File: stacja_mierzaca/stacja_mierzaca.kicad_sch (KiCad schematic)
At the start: 4 parts, among them U1 ESP32-WROOM-32, U2 DS18B20, U3 Ai-Thinker-Ra-02

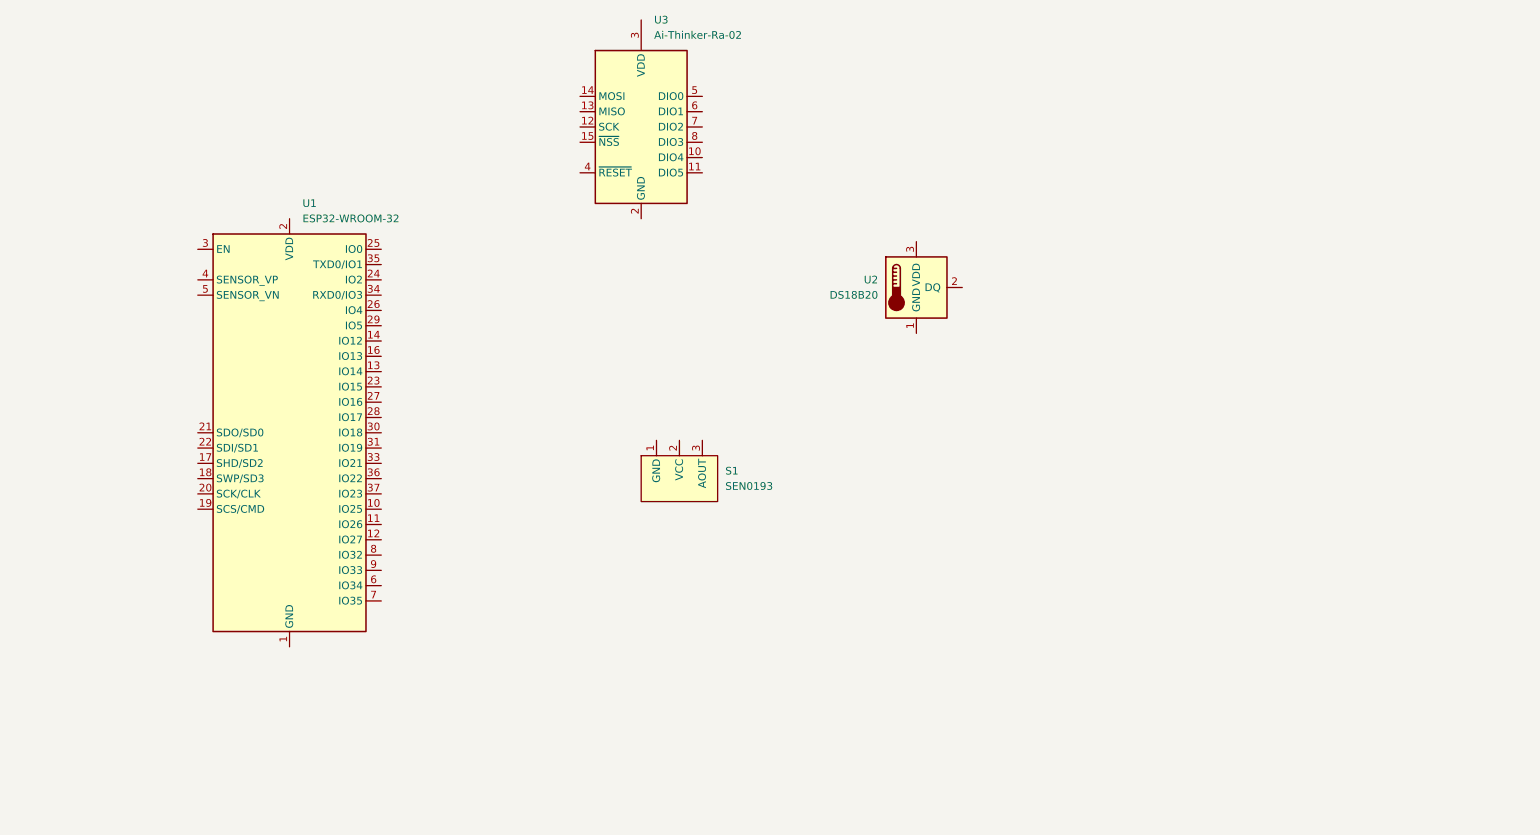
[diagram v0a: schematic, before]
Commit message: feat: add custom esp32 symbol
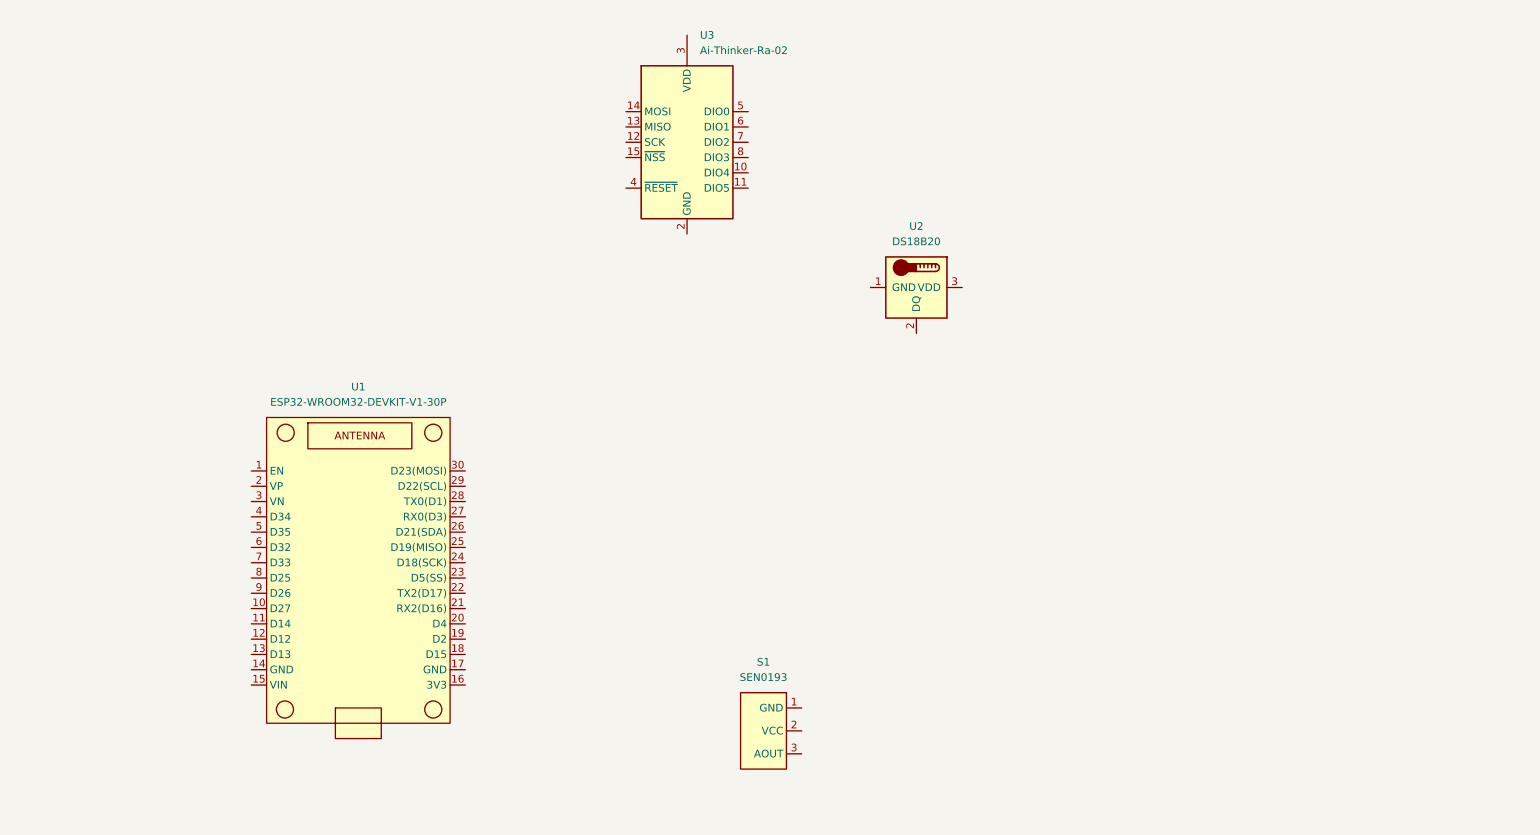
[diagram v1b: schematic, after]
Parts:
- removed U1: ESP32-WROOM-32, RF_Module:ESP32-S2-WROVER, symbol RF_Module:ESP32-WROOM-32
- added U1: ESP32-WROOM32-DEVKIT-V1-30P, symbol custom_sensors:ESP32-WROOM32-DEVKIT-V1-30P
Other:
- moved on the sheet: S1, U2, U3

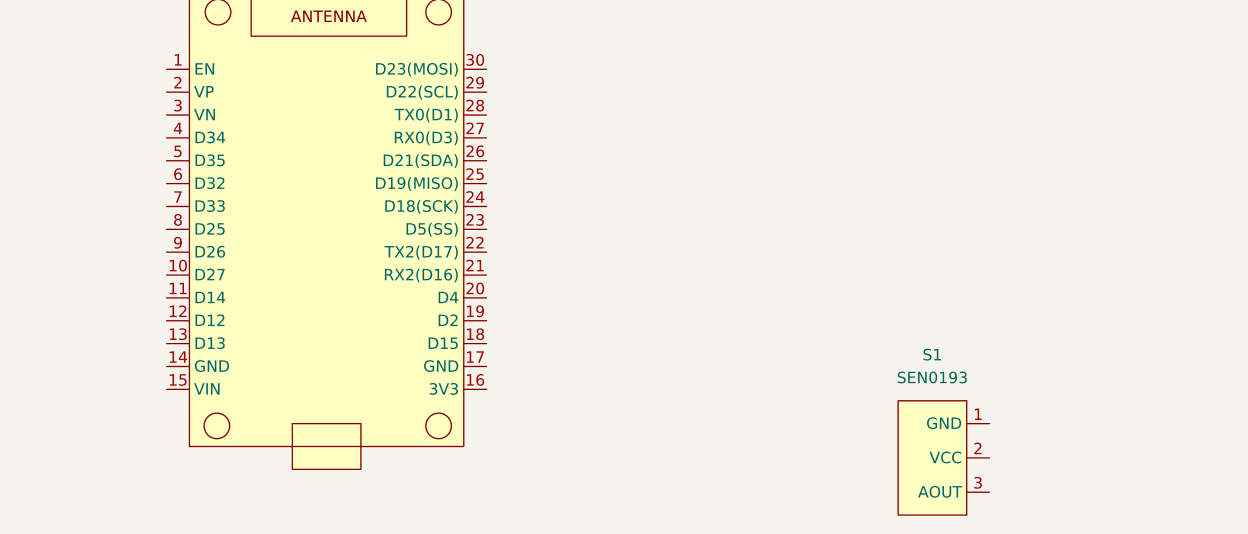
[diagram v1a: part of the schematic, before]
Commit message: feat: connect moisture sensor
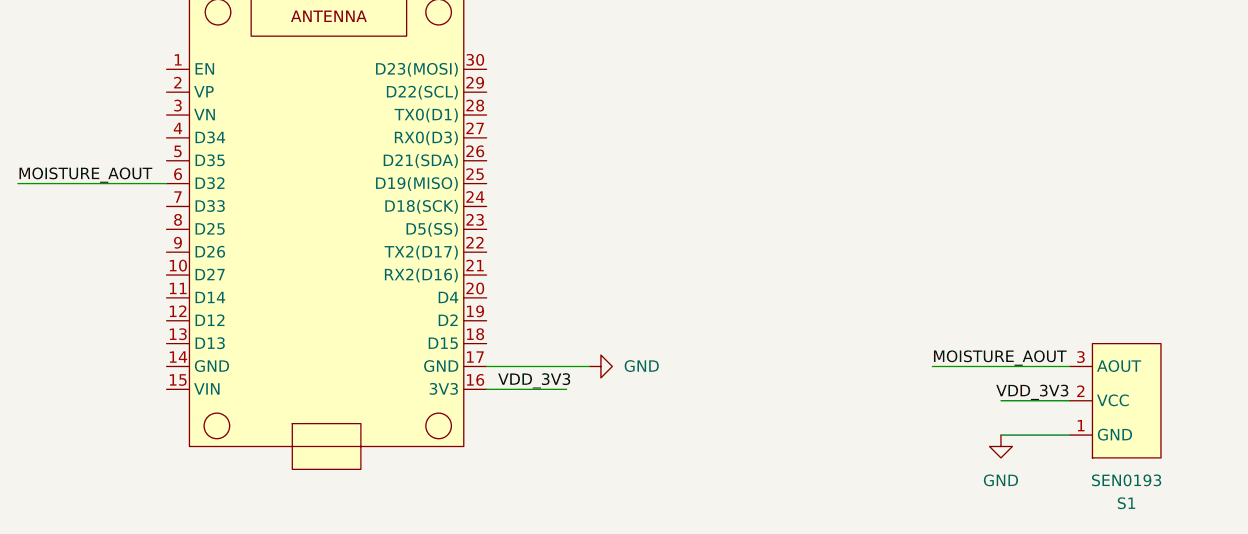
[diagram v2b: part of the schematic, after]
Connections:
- net GND: now reaches S1.1 (GND)
- net GND: now also U1.17 (GND)
- net VDD_3V3: now reaches S1.2 (VCC)
- net VDD_3V3: now also U1.16 (3V3)
- net MOISTURE_AOUT: now reaches S1.3 (AOUT)
- net MOISTURE_AOUT: now also U1.6 (D32)
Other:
- moved on the sheet: S1
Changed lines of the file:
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@@
 		(company "Jan Kubów i Tomasz Gadziński")
+	)
+	(wire
+		(pts
+			(xy 146.05 130.81) (xy 161.29 130.81)
+		)
+		(stroke
+			(width 0)
+			(type default)
+		)
+	)
+	(wire
+		(pts
+			(xy 161.29 138.43) (xy 153.67 138.43)
+		)
+		(stroke
+			(width 0)
+			(type default)
+		)
+	)
+	(wire
+		(pts
+			(xy 96.52 130.81) (xy 107.95 130.81)
+		)
+		(stroke
+			(width 0)
+			(type default)
+		)
+	)
+	(wire
+		(pts
+			(xy 96.52 133.35) (xy 105.41 133.35)
+		)
+		(stroke
+			(width 0)
+			(type default)
+		)
+	)
+	(wire
+		(pts
+			(xy 161.29 134.62) (xy 153.67 134.62)
+		)
+		(stroke
+			(width 0)
+			(type default)
+		)
+	)
+	(wire
+		(pts
+			(xy 44.45 110.49) (xy 60.96 110.49)
+		)
+		(stroke
+			(width 0)
+			(type default)
+		)
+	)
+	(label "MOISTURE_AOUT"
+		(at 146.05 130.81 0)
+		(effects
+			(font
+				(size 1.27 1.27)
+			)
+			(justify left bottom)
+		)
+	)
+	(label "MOISTURE_AOUT"
+		(at 44.45 110.49 0)
+		(effects
+			(font
+				(size 1.27 1.27)
+			)
+			(justify left bottom)
+		)
+	)
+	(label "VDD_3V3"
+		(at 97.79 133.35 0)
+		(effects
+			(font
+				(size 1.27 1.27)
+			)
+			(justify left bottom)
+		)
+	)
+	(label "VDD_3V3"
+		(at 161.29 134.62 180)
+		(effects
+			(font
+				(size 1.27 1.27)
+			)
+			(justify right bottom)
+		)
 	)
 	(symbol
 		(lib_id "custom_sensors:SEN0193")
-		(at 144.78 140.97 270)
+		(at 168.91 134.62 90)
 		(unit 1)
 		(exclude_from_sim no)
@@
 		(fields_autoplaced yes)
 		(property "Reference" "S1"
-			(at 146.05 129.54 90)
+			(at 167.64 146.05 90)
 			(effects
 				(font
@@
 		)
 		(property "Value" "SEN0193"
-			(at 146.05 132.08 90)
+			(at 167.64 143.51 90)
 			(effects
 				(font
@@
 		)
 		(property "Footprint" ""
-			(at 144.78 140.97 0)
+			(at 168.91 134.62 0)
 			(effects
 				(font
@@
 		)
 		(property "Datasheet" ""
-			(at 144.78 140.97 0)
+			(at 168.91 134.62 0)
 			(effects
 				(font
@@
 		)
 		(property "Description" "DFRobot capacitive moisture sensor SEN0193"
-			(at 132.842 140.97 0)
+			(at 180.848 134.62 0)
 			(effects
 				(font
@@
 					(unit 1)
 				)
+			)
+		)
+	)
+	(symbol
+		(lib_id "power:GND")
+		(at 107.95 130.81 90)
+		(unit 1)
+		(exclude_from_sim no)
+		(in_bom yes)
+		(on_board yes)
+		(dnp no)
+		(fields_autoplaced yes)
+		(property "Reference" "#PWR01"
+			(at 114.3 130.81 0)
+			(effects
+				(font
+					(size 1.27 1.27)
+				)
+				(hide yes)
+			)
+		)
+		(property "Value" "GND"
+			(at 111.76 130.8099 90)
+			(effects
+				(font
+					(size 1.27 1.27)
+				)
+				(justify right)
+			)
+		)
+		(property "Footprint" ""
+			(at 107.95 130.81 0)
+			(effects
+				(font
+					(size 1.27 1.27)
+				)
+				(hide yes)
+			)
+		)
+		(property "Datasheet" ""
+			(at 107.95 130.81 0)
+			(effects
+				(font
+					(size 1.27 1.27)
+				)
+				(hide yes)
+			)
+		)
+		(property "Description" "Power symbol creates a global label with name \"GND\" , ground"
+			(at 107.95 130.81 0)
+			(effects
+				(font
+					(size 1.27 1.27)
+				)
+				(hide yes)
+			)
+		)
+		(pin "1"
+		)
+		(instances
+			(project ""
+				(path "/08203ee5-32dd-43d7-8eb6-09a929ab0a23"
+					(reference "#PWR01")
+					(unit 1)
+				)
+			)
+		)
+	)
+	(symbol
+		(lib_id "power:GND")
+		(at 153.67 138.43 0)
+		(unit 1)
+		(exclude_from_sim no)
+		(in_bom yes)
+		(on_board yes)
+		(dnp no)
+		(fields_autoplaced yes)
+		(property "Reference" "#PWR02"
+			(at 153.67 144.78 0)
+			(effects
+				(font
+					(size 1.27 1.27)
+				)
+				(hide yes)
+			)
+		)
+		(property "Value" "GND"
+			(at 153.67 143.51 0)
+			(effects
+				(font
+					(size 1.27 1.27)
+				)
+			)
+		)
+		(property "Footprint" ""
+			(at 153.67 138.43 0)
+			(effects
+				(font
+					(size 1.27 1.27)
+				)
+				(hide yes)
+			)
+		)
+		(property "Datasheet" ""
+			(at 153.67 138.43 0)
+			(effects
+				(font
+					(size 1.27 1.27)
+				)
+				(hide yes)
+			)
+		)
+		(property "Description" "Power symbol creates a global label with name \"GND\" , ground"
+			(at 153.67 138.43 0)
+			(effects
+				(font
+					(size 1.27 1.27)
+				)
+				(hide yes)
+			)
+		)
+		(pin "1"
+		)
+		(instances
+			(project ""
+				(path "/08203ee5-32dd-43d7-8eb6-09a929ab0a23"
+					(reference "#PWR02")
+					(unit 1)
+				)

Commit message: start of load sharing schematic
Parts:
- added BT1: 18650_Cell, symbol Device:Battery_Cell
- added D1: D_Schottky, symbol Device:D_Schottky
- added M1: HW373-TP4056, symbol battery_management:HW373-TP4056
- added Q1: PMOS, symbol Simulation_SPICE:PMOS
- added SC1: Solar_Cell, symbol Device:Solar_Cell
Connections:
- net GND: now also M1.2 (GND), M1.6 (OUT-), SC1.2 (-)
- new net: D1.2 (A), M1.1 (VIN), Q1.2 (G), SC1.1 (+)
- new net: M1.5 (OUT+), Q1.1 (D)
- new net: BT1.1 (+), M1.3 (B+)
- new net: BT1.2 (-), M1.4 (B-)
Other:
- moved on the sheet: S1, U1, U2, U3

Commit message: feat: add rpi scheme
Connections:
- net VDD_3V3: now also U3.3 (VDD)
- net RA02_SCK: now reaches U3.12 (SCK)
- net RA02_SCK: now also U1.24 (D18(SCK))
- net RA02_MISO: now reaches U3.13 (MISO)
- net RA02_MISO: now also U1.25 (D19(MISO))
- net RA02_MOSI: now reaches U3.14 (MOSI)
- net RA02_MOSI: now also U1.30 (D23(MOSI))
- net RA02_SS: now reaches U3.15 (~{NSS})
- net RA02_SS: now also U1.23 (D5(SS))
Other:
- moved on the sheet: S1, U1, U2, U3

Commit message: load sharing schematic finished?
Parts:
- added C1, C2: 33µF, symbol Device:C
- added R1: R100kΩ, symbol Device:R
- added VR1: ~, symbol battery_management:S9V11F5
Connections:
- net GND: now also C1.1, C2.2, R1.2, VR1. (VOUT)
- net SOL_VDD: now reaches D1.2 (A), M1.1 (VIN), Q1.2 (G), SC1.1 (+)
- net SOL_VDD: now also R1.1
- net FET_VDD: now reaches M1.5 (OUT+), Q1.1 (D)
- net CON_VDD: now reaches Q1.3 (S)
- net CON_VDD: now also D1.1 (K), C1.2, VR1. (VOUT)
- net VDD_5V: now reaches U1.15 (VIN)
- new net: C2.1, VR1. (VOUT)
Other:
- moved on the sheet: D1, Q1, SC1

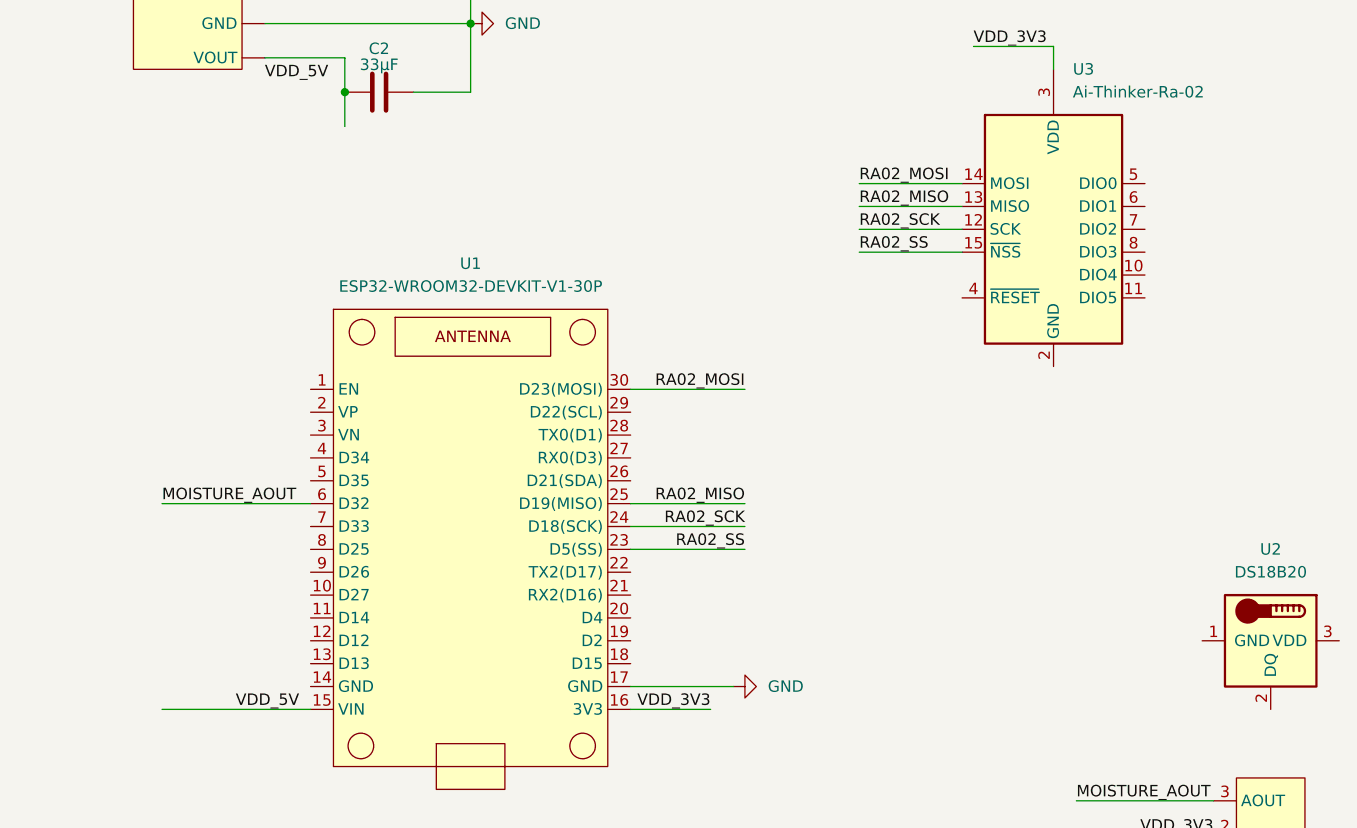
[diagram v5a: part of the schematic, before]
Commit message: feat(esp): add DIO1, DIO0 and RESET connections
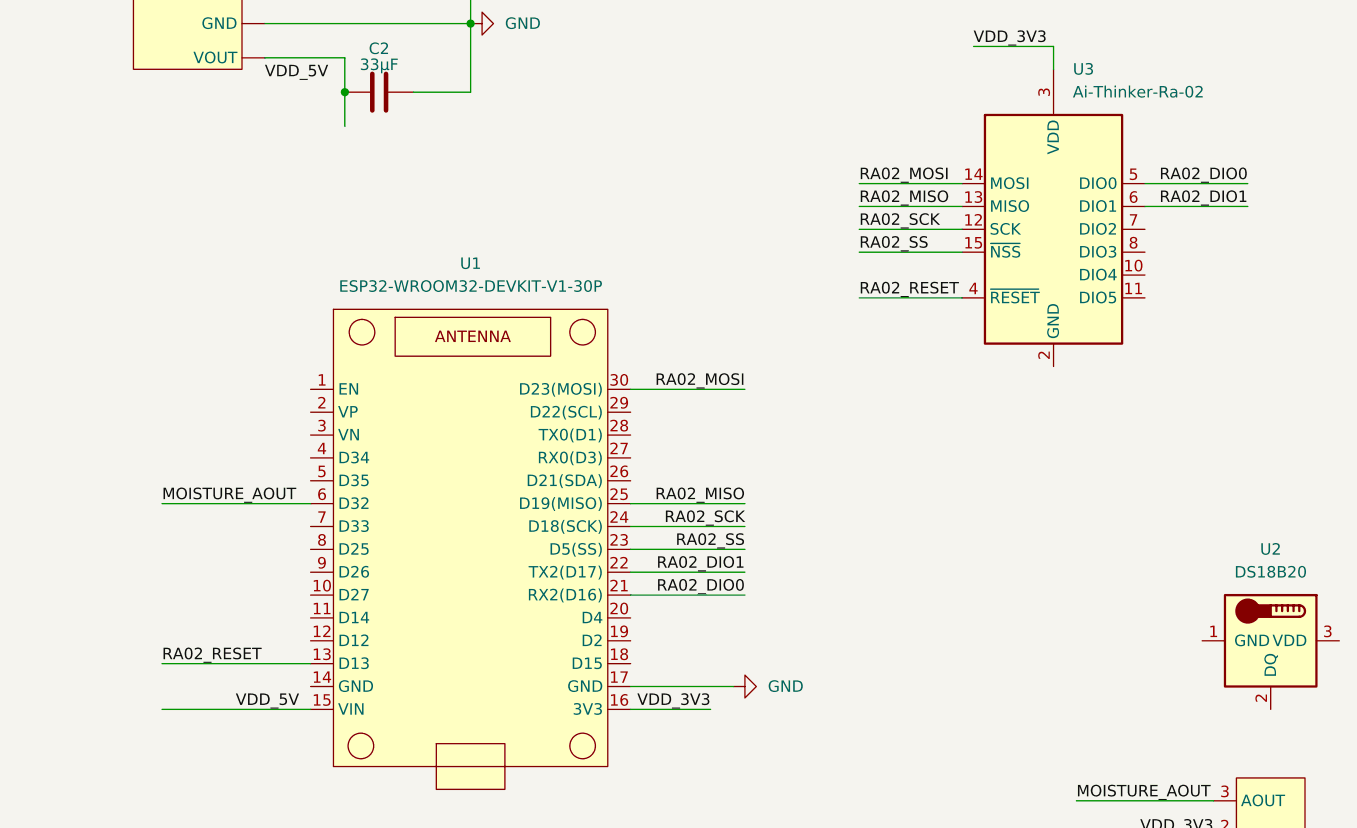
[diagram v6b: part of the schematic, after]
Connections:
- net RA02_RESET: now reaches U3.4 (~{RESET})
- net RA02_RESET: now also U1.13 (D13)
- net RA02_DIO0: now reaches U3.5 (DIO0)
- net RA02_DIO0: now also U1.21 (RX2(D16))
- net RA02_DIO1: now reaches U3.6 (DIO1)
- net RA02_DIO1: now also U1.22 (TX2(D17))
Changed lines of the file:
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@@
+	(wire
+		(pts
+			(xy 138.43 124.46) (xy 154.94 124.46)
+		)
+		(stroke
+			(width 0)
+			(type default)
+		)
+	)
 	(wire
 		(pts
@@
 	(wire
 		(pts
+			(xy 215.9 83.82) (xy 227.33 83.82)
+		)
+		(stroke
+			(width 0)
+			(type default)
+		)
+	)
+	(wire
+		(pts
 			(xy 172.72 60.96) (xy 172.72 53.34)
 		)
@@
 	(wire
 		(pts
+			(xy 247.65 71.12) (xy 259.08 71.12)
+		)
+		(stroke
+			(width 0)
+			(type default)
+		)
+	)
+	(wire
+		(pts
 			(xy 104.14 46.99) (xy 115.57 46.99)
 		)
@@
 	(wire
 		(pts
+			(xy 190.5 116.84) (xy 203.2 116.84)
+		)
+		(stroke
+			(width 0)
+			(type default)
+		)
+	)
+	(wire
+		(pts
+			(xy 247.65 73.66) (xy 259.08 73.66)
+		)
+		(stroke
+			(width 0)
+			(type default)
+		)
+	)
+	(wire
+		(pts
 			(xy 105.41 63.5) (xy 115.57 63.5)
+		)
+		(stroke
+			(width 0)
+			(type default)
+		)
+	)
+	(wire
+		(pts
+			(xy 190.5 114.3) (xy 203.2 114.3)
 		)
 		(stroke
@@
 		)
 	)
+	(label "RA02_DIO0"
+		(at 259.08 71.12 180)
+		(effects
+			(font
+				(size 1.27 1.27)
+			)
+			(justify right bottom)
+		)
+	)
 	(label "RA02_SS"
 		(at 203.2 111.76 180)
@@
 		)
 	)
+	(label "RA02_RESET"
+		(at 215.9 83.82 0)
+		(effects
+			(font
+				(size 1.27 1.27)
+			)
+			(justify left bottom)
+		)
+	)
+	(label "RA02_RESET"
+		(at 138.43 124.46 0)
+		(effects
+			(font
+				(size 1.27 1.27)
+			)
+			(justify left bottom)
+		)
+	)
 	(label "RA02_MOSI"
 		(at 215.9 71.12 0)
@@
 		)
 	)
+	(label "RA02_DIO1"
+		(at 259.08 73.66 180)
+		(effects
+			(font
+				(size 1.27 1.27)
+			)
+			(justify right bottom)
+		)
+	)
 	(label "CON_VDD"
 		(at 106.68 46.99 0)
@@
 		)
 	)
+	(label "RA02_DIO0"
+		(at 203.2 116.84 180)
+		(effects
+			(font
+				(size 1.27 1.27)
+			)
+			(justify right bottom)
+		)
+	)
+	(label "RA02_DIO1"
+		(at 203.2 114.3 180)
+		(effects
+			(font
+				(size 1.27 1.27)
+			)
+			(justify right bottom)
+		)
+	)
